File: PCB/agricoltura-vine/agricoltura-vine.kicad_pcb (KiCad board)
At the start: 4 copper layers, 110 x 80 mm, 148 parts, among them K1 G5LE-14_DC5, K2 G5LE-14_DC5, Q1 IRLML6346TRPBF, Q2 IRLML6346TRPBF, SW1 TL3301NF260QG, T1 BU2032SM-JJ-GTR, T10 BM04B-SRSS-TB(LF)(SN), T11 BM04B-SRSS-TB(LF)(SN), T12 BM04B-SRSS-TB(LF)(SN), T13 BM04B-SRSS-TB(LF)(SN), T14 BM04B-SRSS-TB(LF)(SN), T15 BM04B-SRSS-TB(LF)(SN), T16 0395121002, T17 0395121004, T18 0395121004, T19 TSW-108-07-G-T, T2 20021121-00010C4LF, T20 0010897080, T21 0395121003, T22 0395121003, T3 0675031020, T4 BM04B-SRSS-TB(LF)(SN), T5 BM04B-SRSS-TB(LF)(SN), T6 BM04B-SRSS-TB(LF)(SN), T7 BM04B-SRSS-TB(LF)(SN), T8 BM04B-SRSS-TB(LF)(SN), T9 BM04B-SRSS-TB(LF)(SN), U1 STM32F446RET6, U10 ZXGD3009E6TA, U11 AT24C16D-STUM-T, U2 74HC4052D, U3 TCA9548APWR, U4 AP63203WU-7, U5 AP63205WU-7, U6 MAX13450EAUD+, U7 MAX13450EAUD+, U8 TCA6416ARTWR, U9 ZXGD3009E6TA, X1 ABM3B-8.000MHZ-B2-T, X2 ABS07-32.768KHZ-9-T

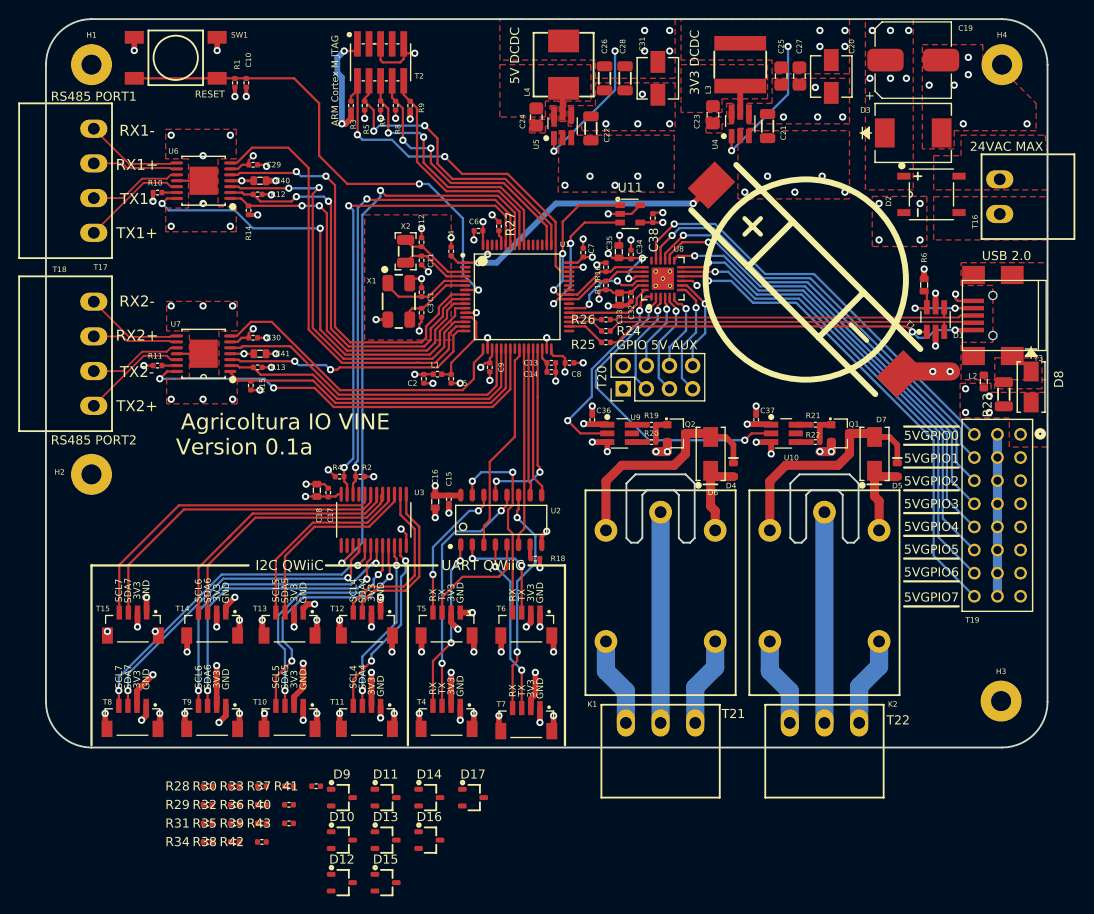
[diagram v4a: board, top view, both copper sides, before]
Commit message: Board tweaks
TVS diodes added, board needs routing, a lot of board has been tweaked, more to come.
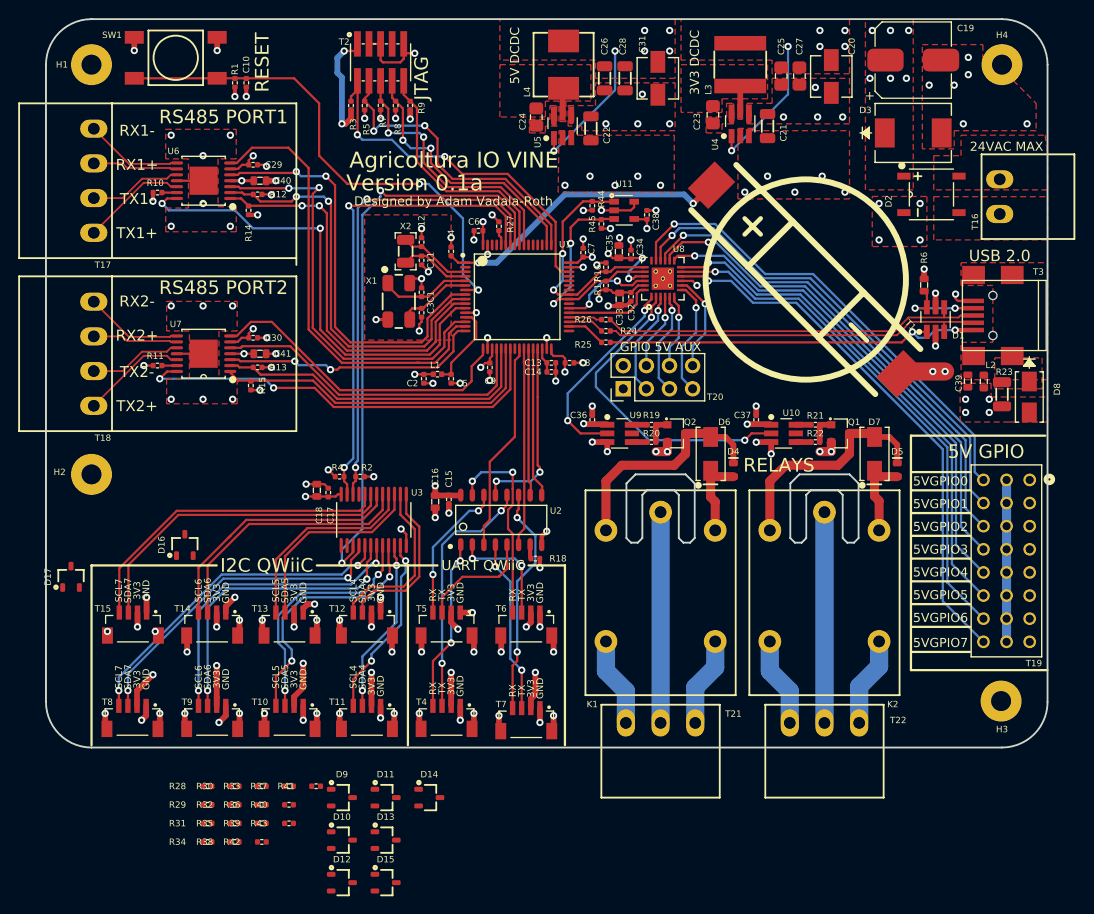
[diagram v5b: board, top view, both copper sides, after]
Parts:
- added C39: C0603X103K1RAC3316, AVR-KiCAD-Lib-Capacitors:C0603, F.Cu at (206.2, 99.8)
- added R44: RC0402FR-074K7L, AVR-KiCAD-Lib-Resistors:R0402, F.Cu at (165.0, 80.5)
- added R45: RC0402FR-074K7L, AVR-KiCAD-Lib-Resistors:R0402, F.Cu at (166.0, 82.5)
- moved D17 50.4 mm to (107.8, 121.2), turned to 90 degrees
- moved D16 42.1 mm to (120.2, 117.8), turned to 90 degrees
- moved T19 5.10 mm to (210.5, 119.5)
- moved D8 1.12 mm to (213.0, 101.5)
- moved U11 0.76 mm to (168.5, 81.0)
- moved C38 0.74 mm to (171.0, 81.5)
- moved R23 0.20 mm to (210.0, 101.2)
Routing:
- net Net-(T19-Pad9): track 48.8 -> 54.2 mm
- net Net-(T19-Pad6): track 48.2 -> 53.7 mm
- net Net-(T19-Pad3): track 47.4 -> 52.8 mm
- net Net-(T19-Pad24): track 54.2 -> 59.6 mm
- net Net-(T19-Pad15): track 49.8 -> 55.2 mm
- net Net-(T19-Pad21): track 52.3 -> 57.7 mm
- net Net-(T19-Pad12): track 49.7 -> 55.1 mm
- net Net-(T19-Pad18): track 50.8 -> 56.2 mm
- net +3V3: track 124.1 -> 128.2 mm, vias 44 -> 46
- net /STM32F446RET Controller/D+: track 41.2 -> 42.2 mm
- net /5V IO Interfaces/P05: track 9.11 -> 8.21 mm
- net /STM32F446RET Controller/VBAT: track 32.4 -> 33.3 mm
- net GND: track 156.6 -> 156.0 mm
- net /I2C Sensor Interfaces/QWIIC_SD5: track 21.5 -> 22.0 mm
- net /I2C Sensor Interfaces/QWIIC_SC5: track 21.6 -> 22.2 mm
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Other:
- board text added: "5V GPIO"
- board text added: "Designed by Adam Vadala-Roth"
- board text added: "JTAG"
- board text added: "RELAYS"
- board text removed: "ARM Cortex M JTAG"

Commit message: TVS Diodes
TVS diodes and pullups added to sensor connectors, implemented in schematic and board.
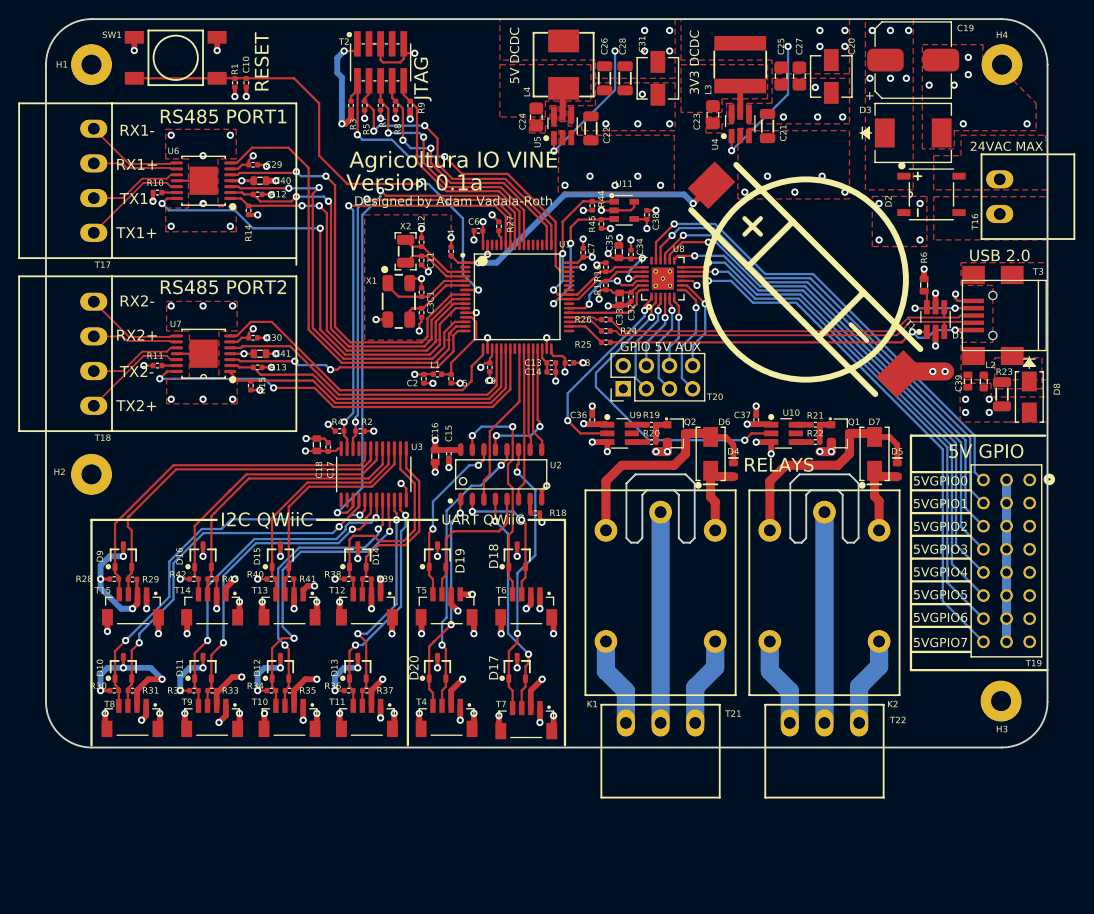
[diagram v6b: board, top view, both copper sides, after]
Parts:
- added D18: PESD3V3L2BT,215, AVR-KiCAD-Lib-Diodes:SOT-23, F.Cu at (156.8, 119.0)
- added D19: PESD3V3L2BT,215, AVR-KiCAD-Lib-Diodes:SOT-23, F.Cu at (148.0, 119.0)
- added D20: PESD3V3L2BT,215, AVR-KiCAD-Lib-Diodes:SOT-23, F.Cu at (148.0, 131.2)
- moved D17 50.0 mm to (156.8, 131.2)
- moved D15 37.7 mm to (130.8, 119.0), turned to 90 degrees
- moved D9 35.8 mm to (113.5, 119.0), turned to 90 degrees
- moved R38 31.5 mm to (138.2, 121.5)
- moved D10 30.6 mm to (113.5, 131.2), turned to 90 degrees
- moved R42 29.8 mm to (121.2, 121.5)
- moved R39 29.2 mm to (140.2, 121.5), turned to 180 degrees
- moved R43 28.1 mm to (123.2, 121.5), turned to 180 degrees
- moved D14 27.6 mm to (139.2, 119.0), turned to 90 degrees
- moved R29 26.1 mm to (114.5, 121.5), turned to 180 degrees
- moved R28 25.0 mm to (112.5, 121.5)
- moved R40 24.9 mm to (129.8, 121.5)
- moved D11 24.6 mm to (122.2, 131.2), turned to 90 degrees
- moved D12 24.5 mm to (130.8, 131.2), turned to 90 degrees
- moved R41 22.9 mm to (131.8, 121.5), turned to 180 degrees
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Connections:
- D10 pad 1: /I2C Sensor Interfaces/QWIIC_SD0 -> /I2C Sensor Interfaces/QWIIC_SC0
- D10 pad 2: /I2C Sensor Interfaces/QWIIC_SC0 -> /I2C Sensor Interfaces/QWIIC_SD0
- D11 pad 1: /I2C Sensor Interfaces/QWIIC_SD1 -> /I2C Sensor Interfaces/QWIIC_SC1
- D11 pad 2: /I2C Sensor Interfaces/QWIIC_SC1 -> /I2C Sensor Interfaces/QWIIC_SD1
- D12 pad 1: /I2C Sensor Interfaces/QWIIC_SD2 -> /I2C Sensor Interfaces/QWIIC_SC2
- D12 pad 2: /I2C Sensor Interfaces/QWIIC_SC2 -> /I2C Sensor Interfaces/QWIIC_SD2
- D13 pad 1: /I2C Sensor Interfaces/QWIIC_SD3 -> /I2C Sensor Interfaces/QWIIC_SC3
- D13 pad 2: /I2C Sensor Interfaces/QWIIC_SC3 -> /I2C Sensor Interfaces/QWIIC_SD3
- D14 pad 1: /I2C Sensor Interfaces/QWIIC_SD4 -> /I2C Sensor Interfaces/QWIIC_SC4
- D14 pad 2: /I2C Sensor Interfaces/QWIIC_SC4 -> /I2C Sensor Interfaces/QWIIC_SD4
- D15 pad 1: /I2C Sensor Interfaces/QWIIC_SD5 -> /I2C Sensor Interfaces/QWIIC_SC5
- D15 pad 2: /I2C Sensor Interfaces/QWIIC_SC5 -> /I2C Sensor Interfaces/QWIIC_SD5
- D16 pad 1: /I2C Sensor Interfaces/QWIIC_SD6 -> /I2C Sensor Interfaces/QWIIC_SC6
- D16 pad 2: /I2C Sensor Interfaces/QWIIC_SC6 -> /I2C Sensor Interfaces/QWIIC_SD6
- D17 pad 1: /I2C Sensor Interfaces/QWIIC_SD7 -> /UART Sensor Interfaces/UARTS4_RX
- D17 pad 2: /I2C Sensor Interfaces/QWIIC_SC7 -> /UART Sensor Interfaces/UARTS4_TX
- D9 pad 1: /I2C Sensor Interfaces/QWIIC_SD7 -> /I2C Sensor Interfaces/QWIIC_SC7
- D9 pad 2: /I2C Sensor Interfaces/QWIIC_SC7 -> /I2C Sensor Interfaces/QWIIC_SD7
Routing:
- net +3V3: track 128.2 -> 190.4 mm, vias 46 -> 66
- net /I2C Sensor Interfaces/QWIIC_SC2: track 27.9 -> 34.4 mm
- net /I2C Sensor Interfaces/QWIIC_SC0: track 37.0 -> 43.4 mm
- net /I2C Sensor Interfaces/QWIIC_SD3: track 19.3 -> 25.6 mm
- net /UART Sensor Interfaces/UARTS4_TX: track 19.1 -> 25.0 mm
- net /I2C Sensor Interfaces/QWIIC_SC3: track 20.2 -> 26.0 mm
- net /UART Sensor Interfaces/UARTS1_RX: track 19.0 -> 24.5 mm
- net /UART Sensor Interfaces/UARTS4_RX: track 25.3 -> 30.8 mm
- net /STM32F446RET Controller/USW1_S0: track 16.2 -> 10.7 mm
- net /I2C Sensor Interfaces/QWIIC_SD2: track 26.8 -> 32.2 mm
- net /I2C Sensor Interfaces/QWIIC_SD0: track 36.1 -> 41.5 mm
- net /I2C Sensor Interfaces/QWIIC_SC4: track 18.6 -> 23.8 mm
- net /I2C Sensor Interfaces/I2C_MUX1_RESET: track 64.4 -> 59.4 mm
- net /STM32F446RET Controller/USW1_S1: track 16.5 -> 11.5 mm
- net /STM32F446RET Controller/USW1_EN: track 22.0 -> 17.0 mm
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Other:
- board text removed: "3V3"
- board text removed: "GND"
- board text removed: "RX"
- board text removed: "SCL4"
- board text removed: "SCL5"
- board text removed: "SCL6"
- board text removed: "SCL7"
- board text removed: "SDA4"
- board text removed: "SDA5"
- board text removed: "SDA6"
- board text removed: "SDA7"
- board text removed: "TX"

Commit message: DC Power
Power input section converted to 24VDC Max input instead of AC. A proper AC to DC power supply would need more components to be properly implmented and not require redesign of the DCDC regulators. Also the plan going forward is to be able to run thes off rechargeable battery packs as well as 24VDC bus voltages.
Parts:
- removed D2: ABS210-13, AVR-KiCAD-Lib-Diodes:ABS210-13
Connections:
- T16 pad 1: /Power Supply/24VAC+ -> +24V
- T16 pad 2: /Power Supply/24VAC- -> GND
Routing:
- net GND: vias 126 -> 128
- net +3V3: vias 66 -> 65
- removed copper zone on F.Cu, net /Power Supply/24VAC+
- removed copper zone on F.Cu, net /Power Supply/24VAC-
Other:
- board text added: "24VDC MAX"
- board text added: "Agricoltura IO VINE-SK"
- board text removed: "24VAC MAX"
- board text removed: "Agricoltura IO VINE"

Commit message: Added license
added license and updated kicad project
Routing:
- net +5V: vias 13 -> 11
- net Earth: vias 0 -> 2
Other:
- net class Default removed
